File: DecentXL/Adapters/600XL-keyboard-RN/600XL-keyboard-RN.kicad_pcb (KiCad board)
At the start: 2 copper layers, 71.6 x 11.2 mm, 25 parts, among them J1 Conn_01x24, J2 Conn_01x24

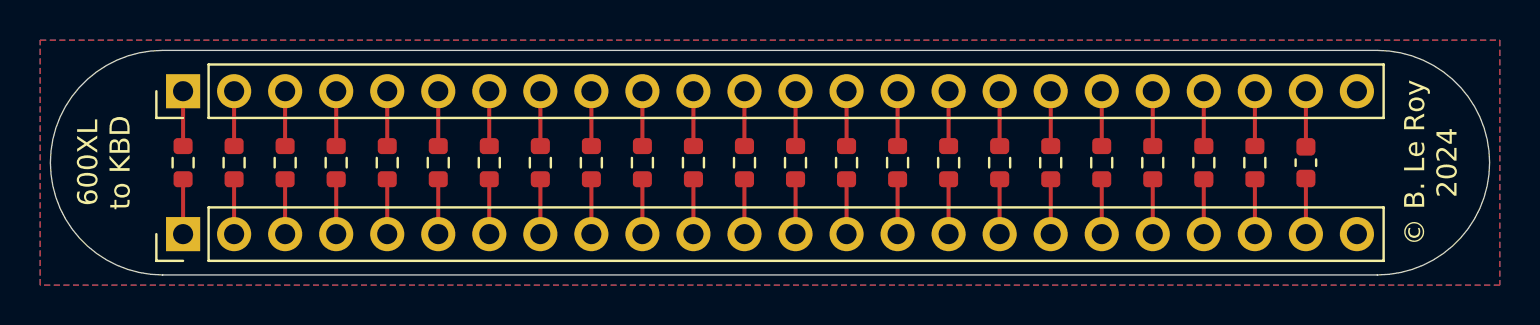
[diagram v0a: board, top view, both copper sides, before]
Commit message: Revision of the 600XL keybaord interface replacement board
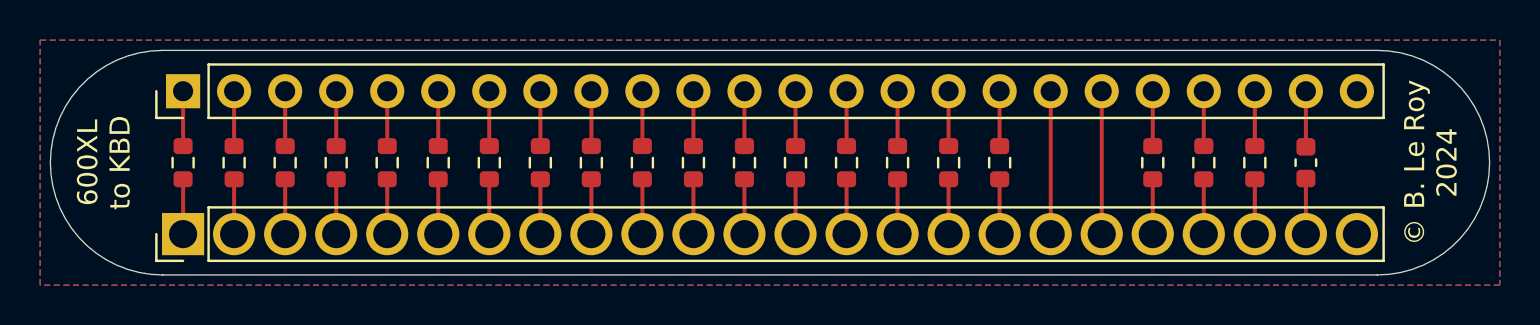
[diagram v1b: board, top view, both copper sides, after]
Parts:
- removed R18, R19: 470, Resistor_SMD:R_0603_1608Metric
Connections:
- J2 pad 18: Net-(J2-Pin_18) -> Net-(J1-Pin_18)
- J2 pad 19: Net-(J2-Pin_19) -> Net-(J1-Pin_19)
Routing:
- net Net-(J1-Pin_19): track 2.73 -> 7.11 mm
- net Net-(J1-Pin_18): track 2.73 -> 7.11 mm
- net Net-(J2-Pin_19): track 2.73 -> 0.00 mm
- net Net-(J2-Pin_18): track 2.73 -> 0.00 mm
